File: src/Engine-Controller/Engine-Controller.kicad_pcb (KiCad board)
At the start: 4 copper layers, 101.6 x 50.8 mm, 57 parts, among them J1 Jumper_NO, P1 EJ508A, P2 USB, P3 SBH11-PBPC-D05-RA-BK, P4 0901471110, P5 66953-005LF, P6 Micro_SD_Card, P7 0901471110, U1 STM32L443VCT6, U2 LM22672MRE-5.0_NOPB, U3 LMS8117AMP-3.3_NOPB, U4 SN74LV07ADR, U5 SST25VF040B-50-4I-S2AE-T, U6 TPS2115APWR

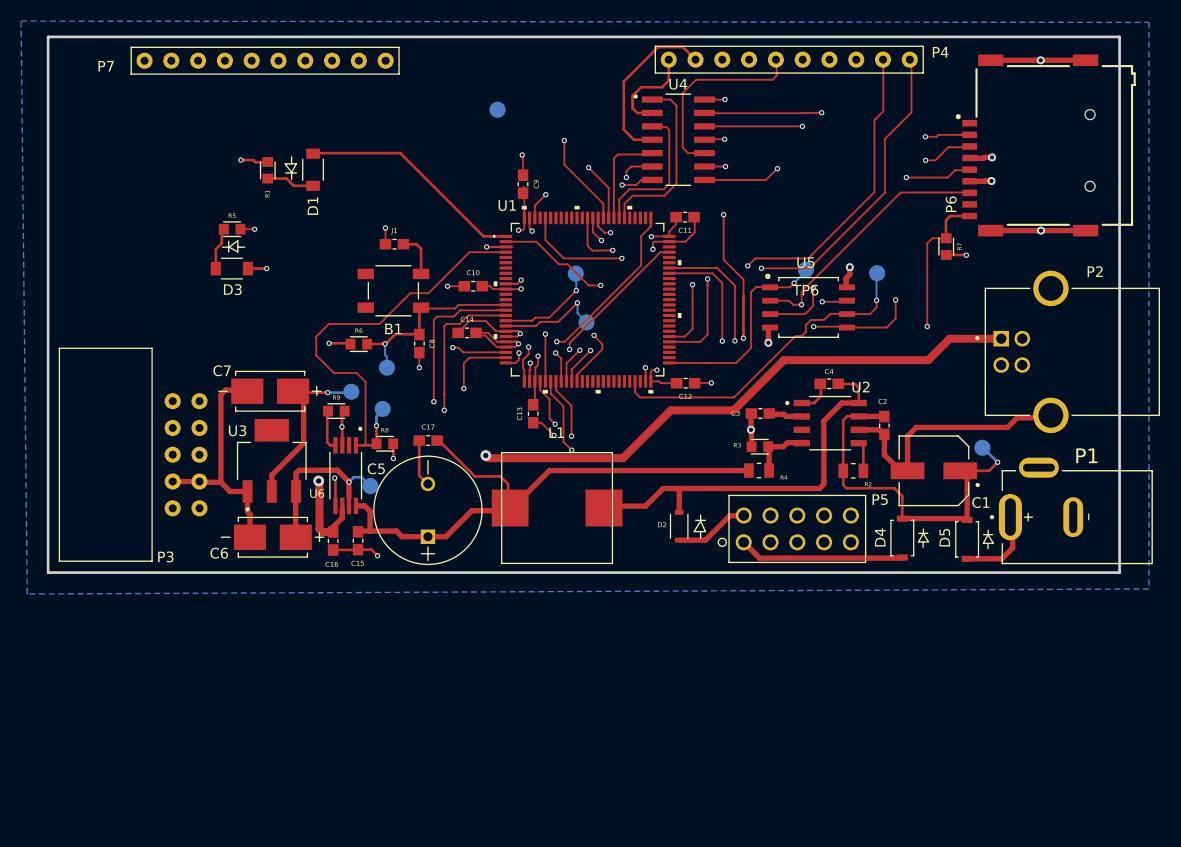
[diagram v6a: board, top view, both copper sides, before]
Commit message: Added silkscreen header labels and SDR Logo
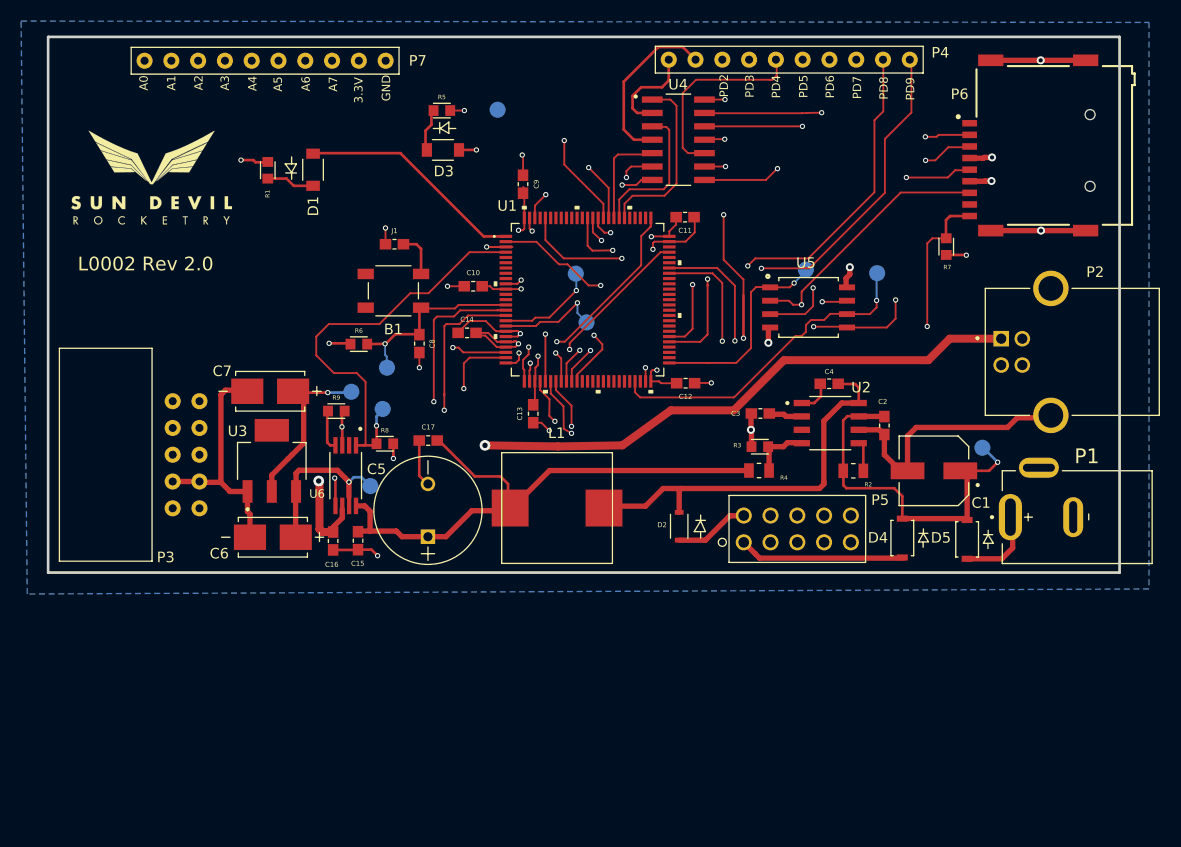
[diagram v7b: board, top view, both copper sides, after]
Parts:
- added G***: LOGO, logo:Logo, F.Cu at (111.4, 114.7)
- moved D3 23.0 mm to (139.0, 112.3)
- moved R5 22.9 mm to (138.9, 108.6)
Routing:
- net Earth: track 133.6 -> 133.0 mm
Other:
- board text added: "3.3V"
- board text added: "A0"
- board text added: "A1"
- board text added: "A2"
- board text added: "A3"
- board text added: "A4"
- board text added: "A5"
- board text added: "A6"
- board text added: "A7"
- board text added: "GND"
- board text added: "L0002 Rev 2.0"
- board text added: "MISO"
- board text added: "MOSI"
- board text added: "PD0"
- board text added: "PD1"
- board text added: "PD2"
- board text added: "PD3"
- board text added: "PD4"
- board text added: "PD5"
- board text added: "PD6"
- board text added: "PD7"
- board text added: "PD8"
- board text added: "PD9"
- board text added: "RX"
- board text added: "SCK"
- board text added: "SCL"
- board text added: "SDA"
- board text added: "SS"
- board text added: "TX"
- board text added: "VIN"
